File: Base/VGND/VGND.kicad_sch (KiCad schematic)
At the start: 35 parts, among them J1 Ground, J2 Barrel_Jack_Switch, J3 Conn_01x03_Pin, J4 Conn_01x03_Pin, J5 AudioJack2_Ground, J6 AudioJack2_Ground, Q1 40V, U1 TLE2426xD, U2 OPA1656

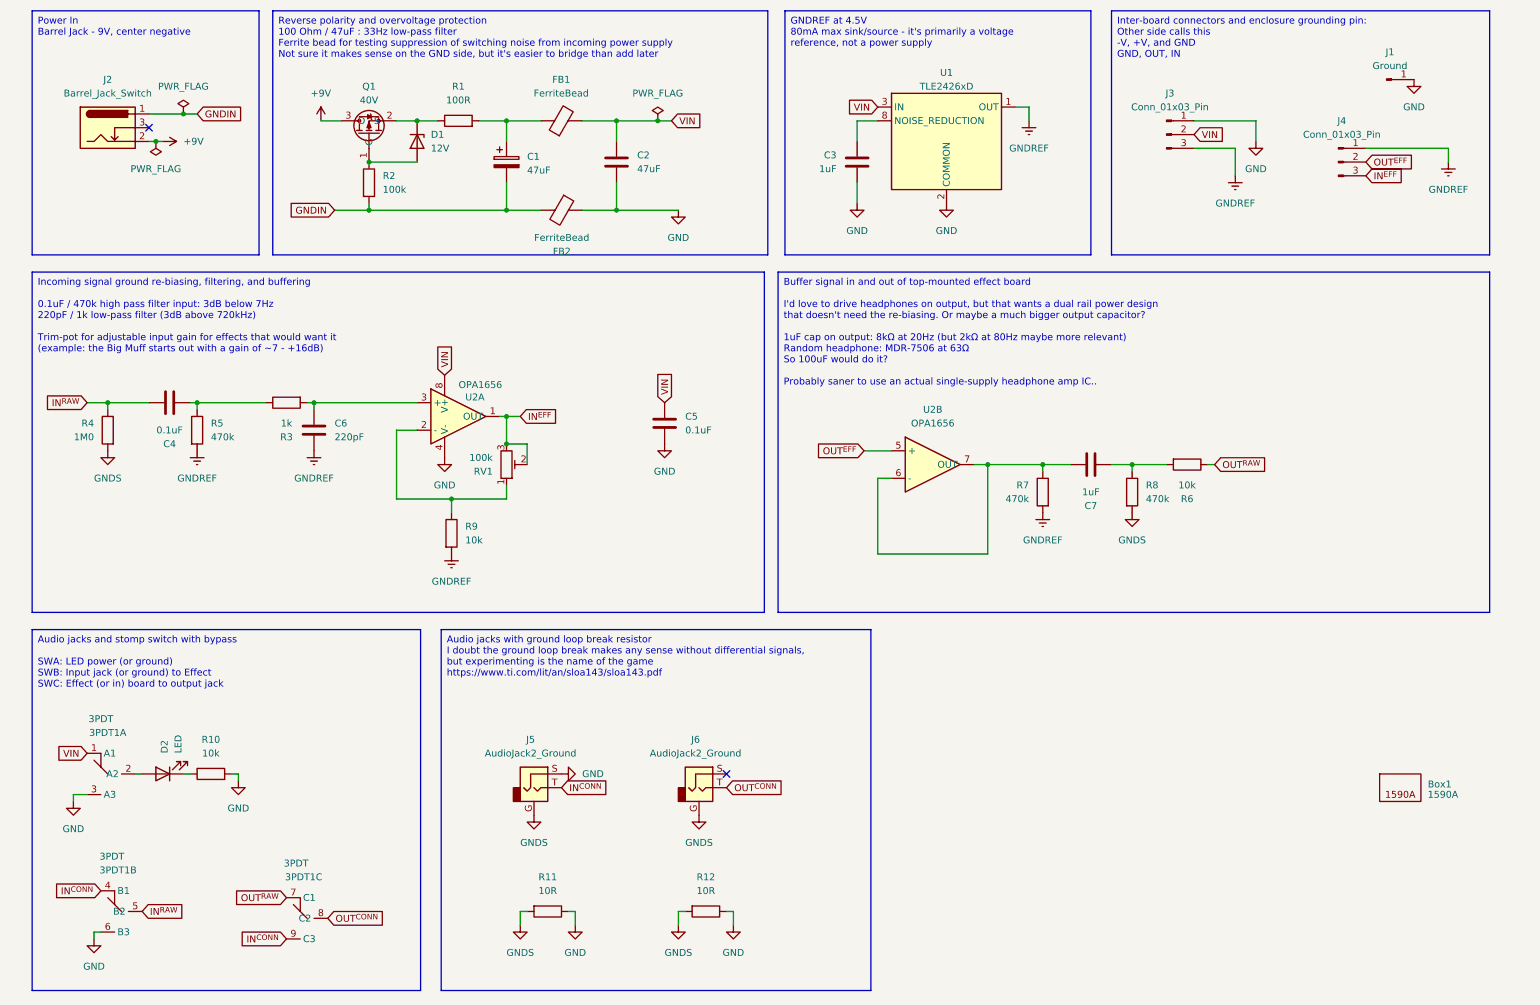
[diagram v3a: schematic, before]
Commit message: Start converting things over to KiCad 9
This does the VGNDA base board.  Apart from the pure conversion thing, I
also ended up:

 - Removing the input gain trim pot again

   Yes, some effects boards might like it, but it's honestly just been a
   pain in general.

 - Adding some SMD status LEDs

   They are on the bottom of the board with the other SMD components, so
   they aren't actually visible when in an enclosure. So pointless.

   But I do most of my testing without any enclosure, and often don't
   solder the actual through-hole stomp switch status LED until later,
   so I've been occasionally annoyed by the complete lack of any visible
   status.

 - Added a "shield" pin to the power connector, because the effects
   board should be able to connect the pot bodies to external ground.

   And it shouldn't use -V or GNDREF, because maybe some day I'll go
   back to a dual supply model. Just make the 3-pin connector be a 4-pin
   one, with the old pins in all the old places, so that old effect
   boards will still work just fine and just not use the new shield pin.

 - Made the grounding pin be a mounting hole instead, because I should
   try to ground the enclosure too, and the grounding pin wasn't great
   for that.

There migth be some other minor edits too, but the base board has
generally been working fine.

One downside to moving to KiCad 9 is that the via stitching plugin
hasn't been updated for the new version yet, so this doesn't stitch the
groundplane.  Not that it was likely to ever matter, but I just like
using GND stitching - particularly when it means not having to add any
manual via connections for some otherwise unconnected GND part.

Signed-off-by: Linus Torvalds <torvalds@linux-foundation.org>
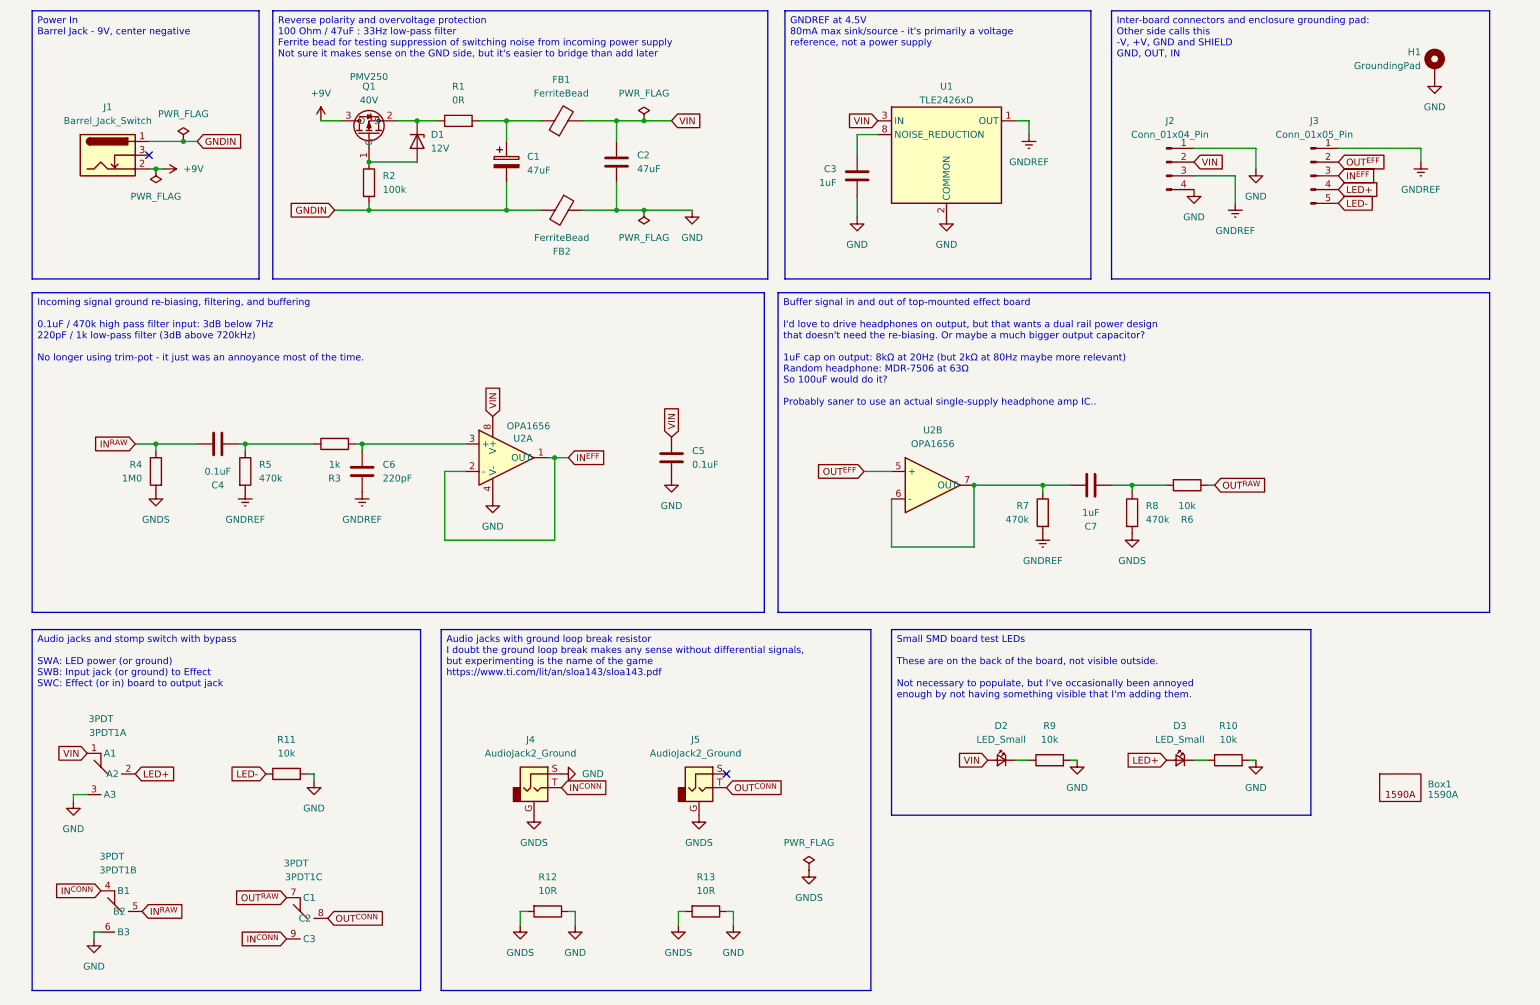
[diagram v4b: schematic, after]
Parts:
- removed D2: LED, LED_THT:LED_D3.0mm, symbol Device:LED
- removed J1: Ground, Connector_PinHeader_2.54mm:PinHeader_1x01_P2.54mm_Vertical, symbol Connector:Conn_01x01_Pin
- removed J3, J4: Conn_01x03_Pin, Connector_PinHeader_2.54mm:PinHeader_1x03_P2.54mm_Vertical, symbol Connector:Conn_01x03_Pin
- removed RV1: 100k, Mylib:Bourns_3362S, symbol Device:R_Potentiometer_Trim
- added D2, D3: LED_Small, LED_SMD:LED_0805_2012Metric_Pad1.15x1.40mm_HandSolder, symbol Device:LED_Small
- added H1: GroundingPad, MountingHole:MountingHole_2.2mm_M2_Pad_Via, symbol Mechanical:MountingHole_Pad
- added J2: Conn_01x04_Pin, Connector_PinSocket_2.54mm:PinSocket_1x04_P2.54mm_Vertical, symbol Connector:Conn_01x04_Pin
- added J3: Conn_01x05_Pin, Connector_PinSocket_2.54mm:PinSocket_1x05_P2.54mm_Vertical, symbol Connector:Conn_01x05_Pin
- added R10: 10k, Resistor_SMD:R_0805_2012Metric_Pad1.20x1.40mm_HandSolder, symbol Device:R
- C1: footprint Capacitor_THT:CP_Radial_D4.0mm_P2.00mm -> Capacitor_THT:CP_Radial_D5.0mm_P2.00mm
- Q1: footprint SOT-23-3 -> Package_TO_SOT_SMD:SOT-23
- R1: value 100R -> 0R
- renumbered J2 to J1, J5 to J4, J6 to J5, R10 to R11, R11 to R12, R12 to R13
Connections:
- net GND: now also R9.2, H1.1, J2.1 (Pin_1), J2.4 (Pin_4), R10.2
- net GNDREF: now also J2.3 (Pin_3), J3.1 (Pin_1); no longer R9.2
- net IN^{EFF}: now also U2.2 (-), J3.3 (Pin_3)
- net OUT^{EFF}: now also J3.2 (Pin_2)
- net VIN: now also D2.2 (A), J2.2 (Pin_2)
- net LED-: now reaches R11.1
- net LED-: now also J3.5 (Pin_5)
- net LED+: now reaches 3PDT1.2 (A2)
- net LED+: now also D3.2 (A), J3.4 (Pin_4)
- net at R9.1: now also D2.1 (K); no longer U2.2 (-)
- new net: D3.1 (K), R10.1
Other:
- moved on the sheet: C3, C4, C5, C6, C7, J1, R11, R3, R4, R5, R6, R7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

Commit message: VGND: misc KiCad-9 noise
Some manual via stitching - still waiting for the scripts to be updated
- and some library symbol changes that seem to be related to just minor
change sin KiCad 9.

Signed-off-by: Linus Torvalds <torvalds@linux-foundation.org>
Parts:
- Q1: footprint Package_TO_SOT_SMD:SOT-23 -> Package_TO_SOT_SMD:SOT-23-3
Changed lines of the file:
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@@
 			)
 		)
-		(property "Footprint" "Package_TO_SOT_SMD:SOT-23"
+		(property "Footprint" "Package_TO_SOT_SMD:SOT-23-3"
 			(at 68.58 44.958 0)
 			(effects

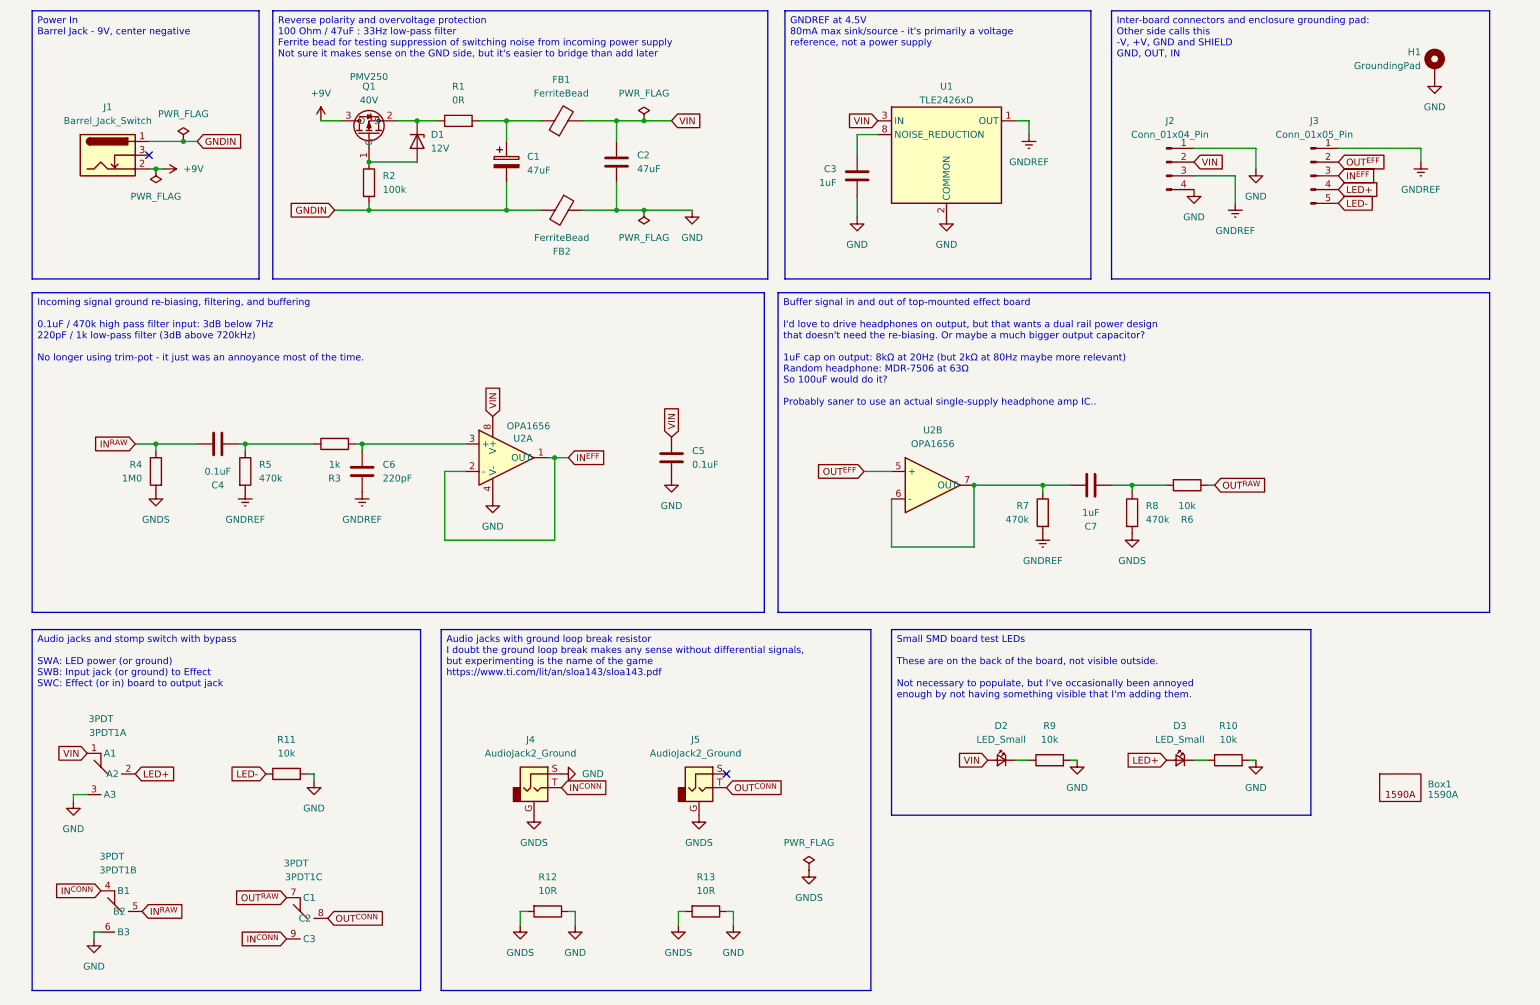
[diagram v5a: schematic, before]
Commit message: Update the VGND board for things from the digital board
This brings the VGND board up to where the digital board was, and also
adds a common mode choke for more power cleaning testing (I know I said
I should do it for the USB-C power board, and I will, but I did it here
too just because I was updating things).

I think I'll try to actively hunt for a couple of cheap and hopefully
bad wall wart guitar power supplies.  Considering how many people
complain about bad guitar power supplies, it should hopefully be easy.

Will the choke matter? I have no idea, but hey, that's kind of the
point, isn't it?

This also adds in the simulation so that you can see the signal
rebiasing happening.  As usual ltspice randomly gives errors that come
and go depending on "use initial conditions" and timing, but when it
works it works.

Signed-off-by: Linus Torvalds <torvalds@linux-foundation.org>
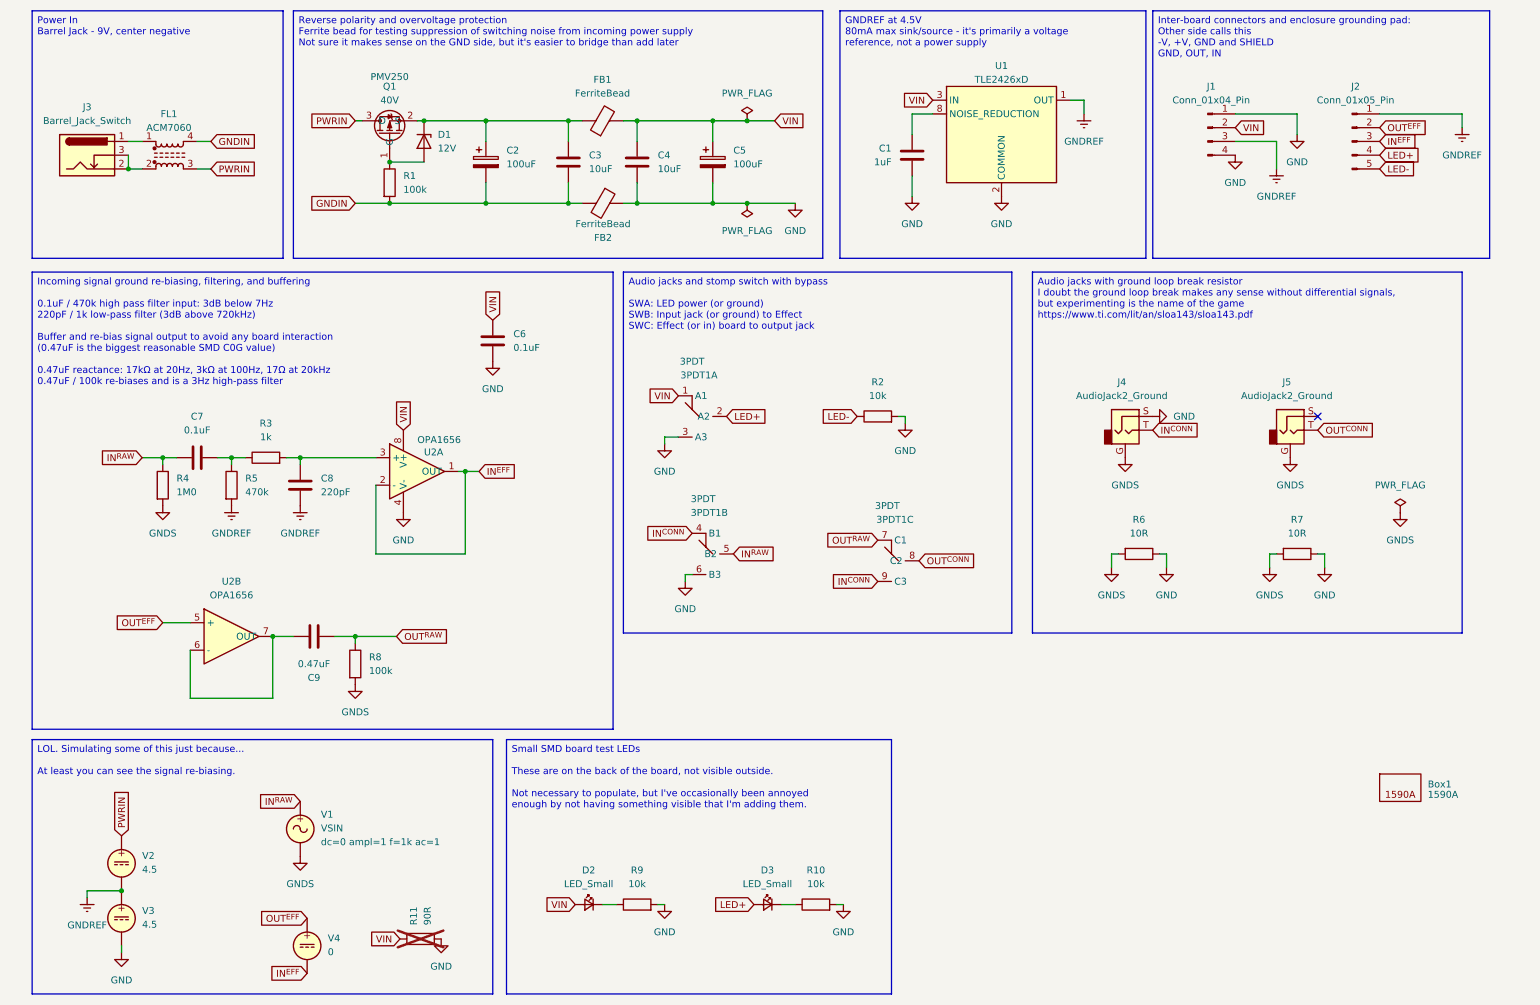
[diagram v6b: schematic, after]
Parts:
- removed C1: 47uF, Capacitor_THT:CP_Radial_D5.0mm_P2.00mm, symbol Device:C_Polarized
- removed H1: GroundingPad, MountingHole:MountingHole_2.2mm_M2_Pad_Via, symbol Mechanical:MountingHole_Pad
- removed R1: 0R, Resistor_SMD:R_0805_2012Metric_Pad1.20x1.40mm_HandSolder, symbol Device:R
- removed R6: 10k, Resistor_SMD:R_0805_2012Metric_Pad1.20x1.40mm_HandSolder, symbol Device:R
- removed R7: 470k, Resistor_SMD:R_0805_2012Metric_Pad1.20x1.40mm_HandSolder, symbol Device:R
- added C2, C5: 100uF, Capacitor_THT:CP_Radial_D8.0mm_P3.50mm, symbol Device:C_Polarized
- added C3: 10uF, Capacitor_SMD:C_1206_3216Metric_Pad1.33x1.80mm_HandSolder, symbol Device:C
- added FL1: ACM7060, Inductor_SMD:L_CommonModeChoke_TDK_ACM7060, symbol Filter:Choke_CommonMode_FerriteCore_1423
- added R11: 90R, symbol Device:R
- added V1: VSIN, symbol Simulation_SPICE:VSIN
- added V2, V3: 4.5, symbol Simulation_SPICE:VDC
- added V4: 0, symbol Simulation_SPICE:VDC
- C4: renamed from C2; value 47uF -> 10uF
- C9: renamed from C7; value 1uF -> 0.47uF
- R8: value 470k -> 100k
- renumbered C3 to C1, C5 to C6, C4 to C7, C6 to C8, J2 to J1, J3 to J2, J1 to J3, R2 to R1, R11 to R2, R12 to R6, R13 to R7
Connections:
- net GND: now also C5.2, R11.2, V3.2
- net GNDIN: now also C2.2, C3.2, FL1.4; no longer J3.1
- net GNDREF: now also V2.2, V3.1
- net GNDS: now also V1.2
- net IN^{EFF}: now also V4.2
- net IN^{RAW}: now also V1.1
- net OUT^{EFF}: now also V4.1
- net OUT^{RAW}: now also C9.1, R8.1
- net VIN: now also C5.1, R11.1
- net at FB1.1: now also D1.1 (K), Q1.2 (S), C2.1, C3.1
- net at J3.3: now also J3.2, FL1.2
- net +9V renamed PWRIN
- net PWRIN: now also FL1.3, V2.1; no longer J3.2
- new net: FL1.1, J3.1
- no-connect marks 2 -> 1
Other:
- moved on the sheet: 3PDT1A, 3PDT1B, 3PDT1C, C1, C4, C6, C7, C8, C9, D1, D2, D3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
